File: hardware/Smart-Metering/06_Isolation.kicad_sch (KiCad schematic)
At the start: 25 parts, among them U601 ISO7741, U602 ISO7742, U603 ISO7740, U604 MCP3204, U605 TPS7A2033

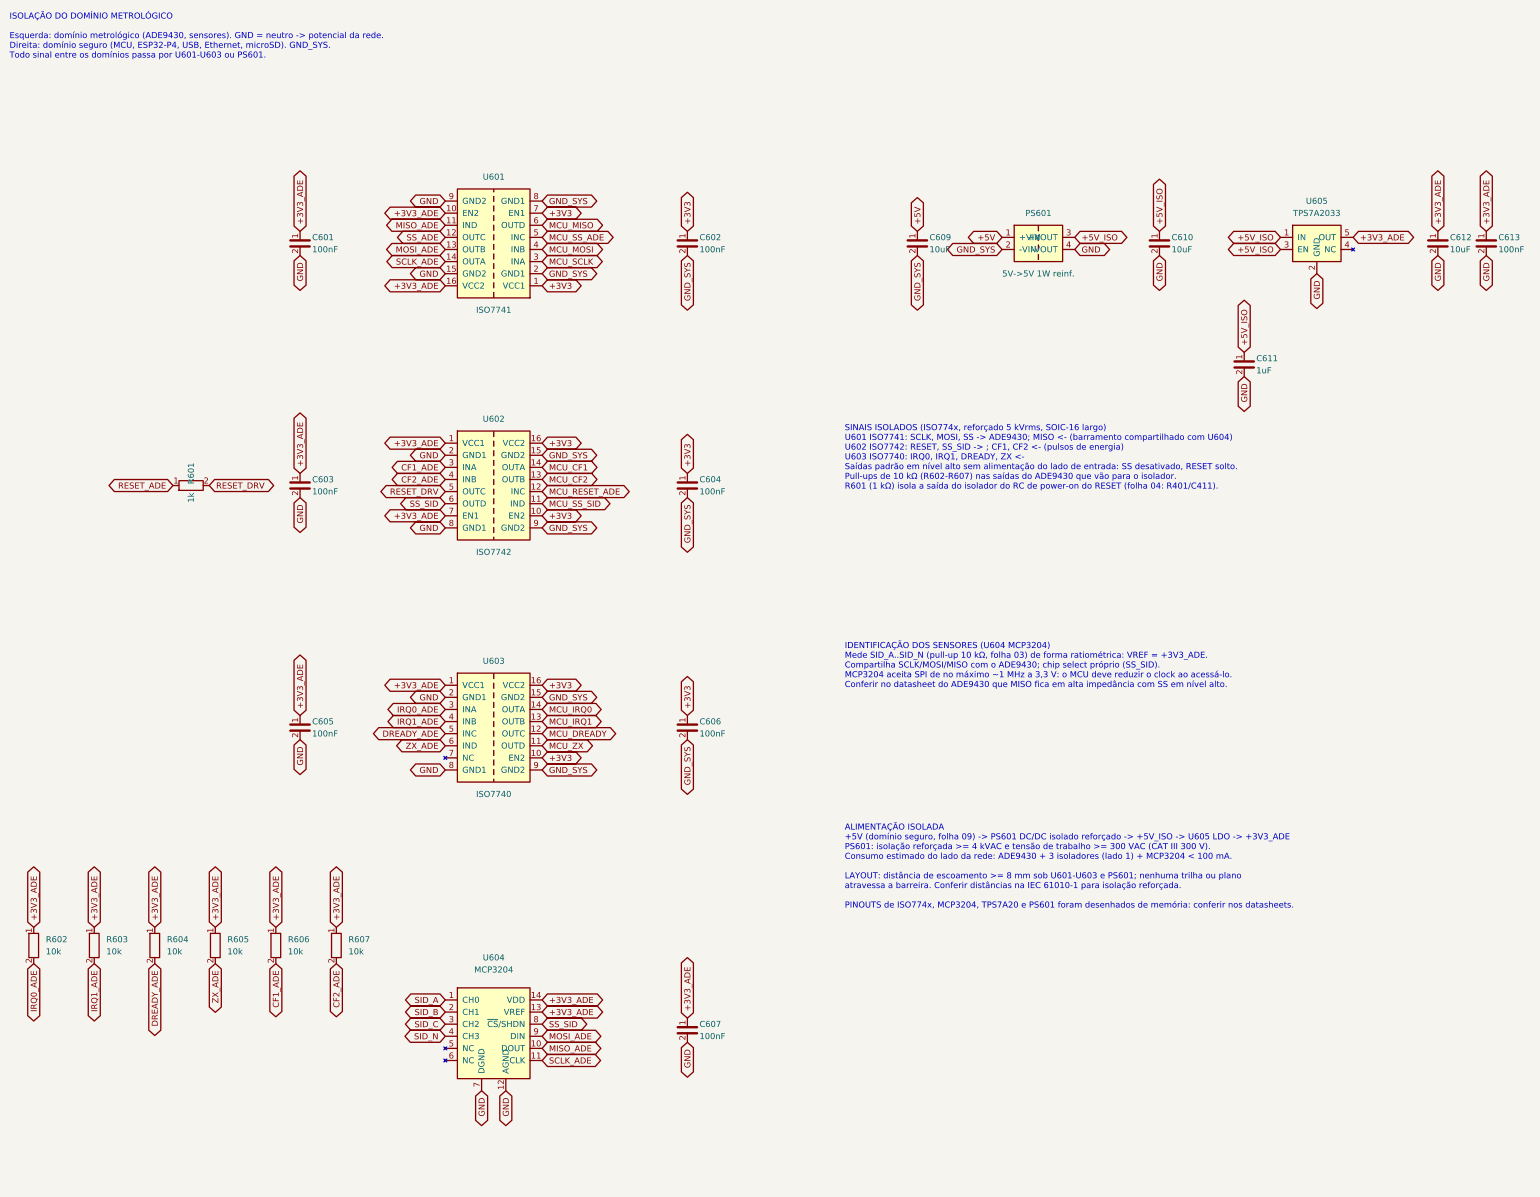
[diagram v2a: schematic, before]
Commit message: Usa símbolos oficiais do KiCad nas folhas de isolação e alimentação
Os símbolos oficiais da biblioteca KiCad 10 (gitlab.com/kicad/libraries)
substituem os desenhados de memória:

- 06_Isolation: ISO7762DW (4/2) e ISO7761DW (5/1) no lugar de três
  ISO774x; os 12 sinais cabem em dois isoladores reforçados. MCP3204 e
  TPS7A20xxxDBV oficiais (os pinouts anteriores conferiram).
- 09_Power_Supplies: BQ24074RGT oficial revelou que o pino 15 é ITERM,
  não SYSOFF; agora tem R911 (3,01 kΩ, fim de carga ≈ 90 mA). +3V3 passa
  ao TPS63001 (buck-boost 3,3 V fixo) e +5V ao TPS61089, com resistores
  de frequência, limite de corrente e compensação a confirmar no WEBENCH.

Símbolos próprios que deixaram de ser usados foram removidos da
biblioteca SmartMetering.

Co-Authored-By: Claude Opus 5.5 <noreply@anthropic.com>
Claude-Session: https://claude.ai/code/session_012B8cVkhtjf3eg98UdpNCpf
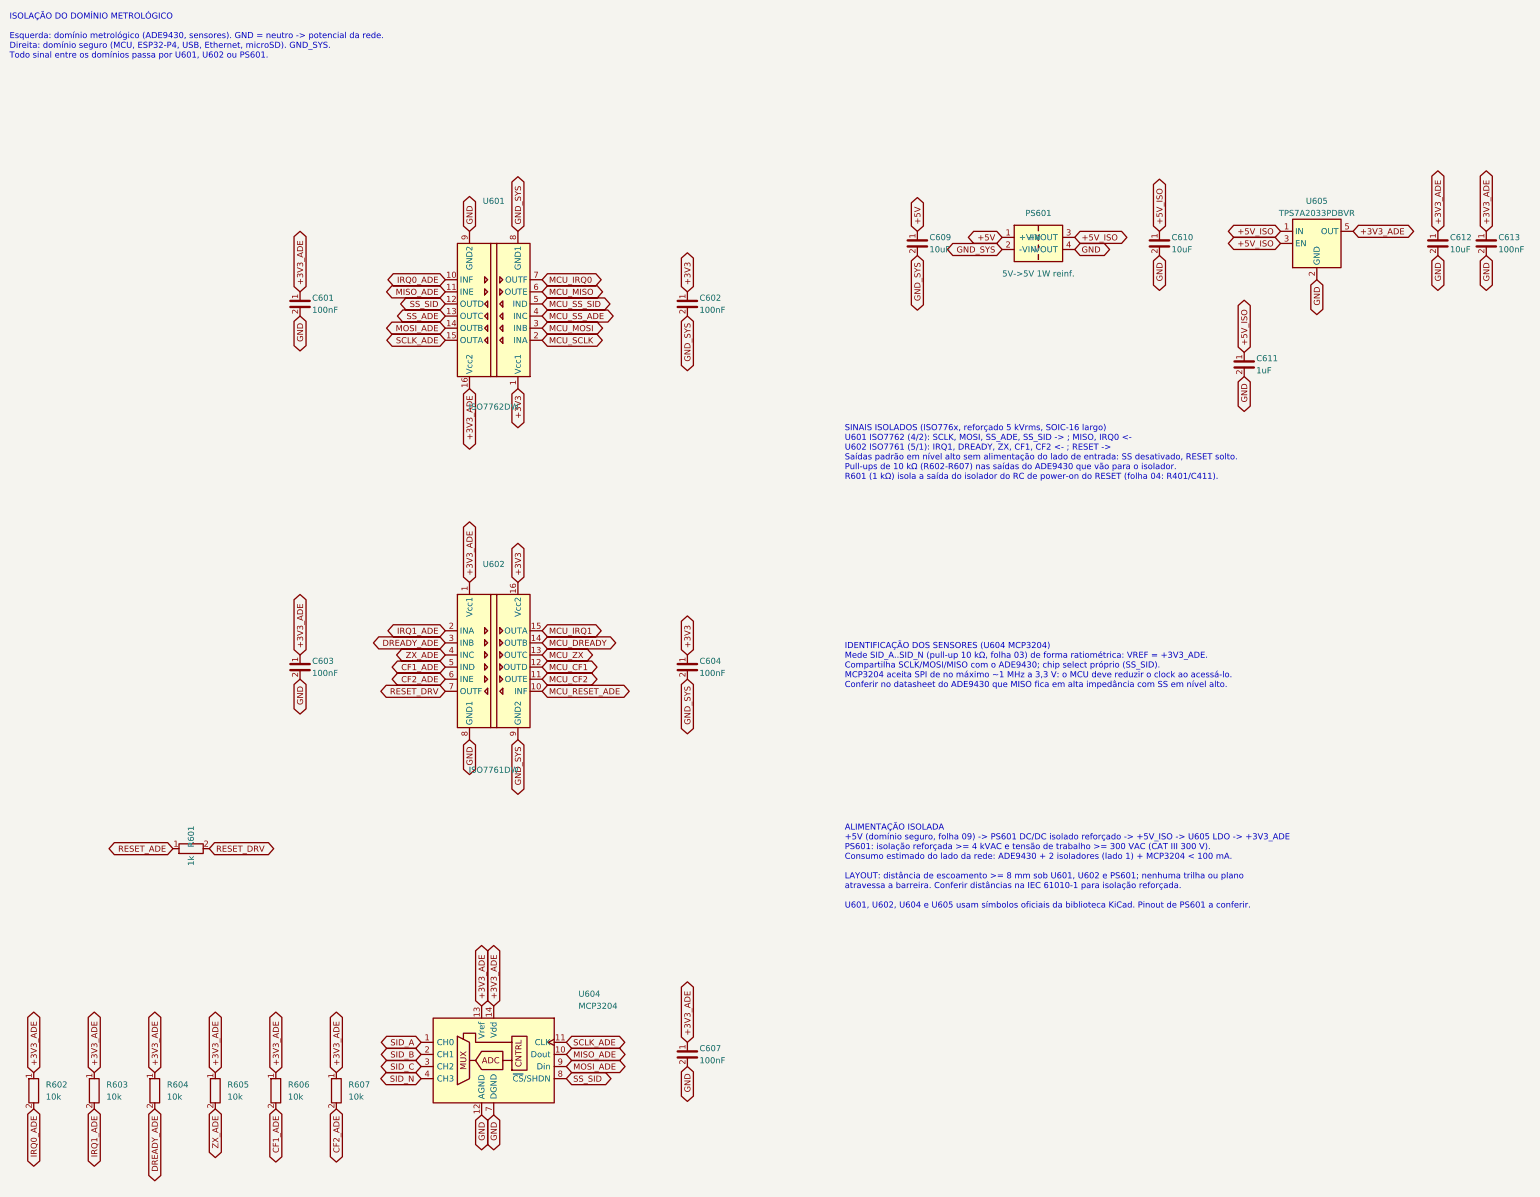
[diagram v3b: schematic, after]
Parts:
- removed C605, C606: 100nF, Capacitor_SMD:C_0603_1608Metric, symbol SmartMetering:C_Vert
- removed U601: ISO7741, Package_SO:SOIC-16W_7.5x10.3mm_P1.27mm, symbol SmartMetering:ISO7741
- removed U602: ISO7742, Package_SO:SOIC-16W_7.5x10.3mm_P1.27mm, symbol SmartMetering:ISO7742
- removed U603: ISO7740, Package_SO:SOIC-16W_7.5x10.3mm_P1.27mm, symbol SmartMetering:ISO7740
- removed U604: MCP3204, Package_SO:SOIC-14_3.9x8.7mm_P1.27mm, symbol SmartMetering:MCP3204
- removed U605: TPS7A2033, Package_TO_SOT_SMD:SOT-23-5, symbol SmartMetering:LDO_EN_SOT23-5
- added U601: ISO7762DW, Package_SO:SOIC-16W_7.5x10.3mm_P1.27mm, symbol Isolator:ISO7762DW
- added U602: ISO7761DW, Package_SO:SOIC-16W_7.5x10.3mm_P1.27mm, symbol Isolator:ISO7761DW
- added U604: MCP3204, Package_SO:SOIC-14_3.9x8.7mm_P1.27mm, symbol Analog_ADC:MCP3204
- added U605: TPS7A2033PDBVR, Package_TO_SOT_SMD:SOT-23-5, symbol Regulator_Linear:TPS7A20xxxDBV
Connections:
- net +3V3: now also U601.1 (Vcc1), U602.16 (Vcc2)
- net +3V3_ADE: now also U601.16 (Vcc2), U602.1 (Vcc1), U604.13 (Vref), U604.14 (Vdd), U605.5 (OUT)
- net +5V_ISO: now also U605.1 (IN), U605.3 (EN)
- net CF1_ADE: now also U602.5 (IND)
- net CF2_ADE: now also U602.6 (INE)
- net DREADY_ADE: now also U602.3 (INB)
- net GND: now also U601.9 (GND2), U602.8 (GND1), U604.12 (AGND), U604.7 (DGND), U605.2 (GND)
- net GND_SYS: now also U601.8 (GND1), U602.9 (GND2)
- net IRQ0_ADE: now also U601.10 (INF)
- net IRQ1_ADE: now also U602.2 (INA)
- net MCU_CF1: now also U602.12 (OUTD)
- net MCU_CF2: now also U602.11 (OUTE)
- net MCU_DREADY: now also U602.14 (OUTB)
- net MCU_IRQ0: now also U601.7 (OUTF)
- net MCU_IRQ1: now also U602.15 (OUTA)
- net MCU_MISO: now also U601.6 (OUTE)
- net MCU_MOSI: now also U601.3 (INB)
- net MCU_RESET_ADE: now also U602.10 (INF)
- net MCU_SCLK: now also U601.2 (INA)
- net MCU_SS_ADE: now also U601.4 (INC)
- net MCU_SS_SID: now also U601.5 (IND)
- net MCU_ZX: now also U602.13 (OUTC)
- net MISO_ADE: now also U601.11 (INE), U604.10 (Dout)
- net MOSI_ADE: now also U601.14 (OUTB), U604.9 (Din)
- net RESET_DRV: now also U602.7 (OUTF)
- net SCLK_ADE: now also U601.15 (OUTA), U604.11 (CLK)
- net SID_A: now also U604.1 (CH0)
- net SID_B: now also U604.2 (CH1)
- net SID_C: now also U604.3 (CH2)
- net SID_N: now also U604.4 (CH3)
- net SS_ADE: now also U601.13 (OUTC)
- net SS_SID: now also U601.12 (OUTD), U604.8 (~{CS}/SHDN)
- net ZX_ADE: now also U602.4 (INC)
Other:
- note added: "ALIMENTAÇÃO ISOLADA +5V (domínio seguro, folha 09) -> PS601 DC/DC isolado reforçado -> +5V_ISO -> U605 LDO -> +3V3_ADE PS601: isolação reforçada >= 4 kVAC e tensão de trabalho >= 300 VAC (CAT III 300 V). Consumo estimado do lado da rede: ADE9430 + 2 isoladores (lado 1) + MCP3204 < 100 mA. LAYOUT: distância de escoamento >= 8 mm sob U601, U602 e PS601; nenhuma trilha ou plano atravessa a barreira.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"
- note added: "ISOLAÇÃO DO DOMÍNIO METROLÓGICO Esquerda: domínio metrológico (ADE9430, sensores). GND = neutro -> potencial da rede. Direita: domínio seguro (MCU, ESP32-P4, USB, Ethernet, microSD). GND_SYS. Todo sinal entre os domínios passa por U601, U602 ou PS601."
- note added: "SINAIS ISOLADOS (ISO776x, reforçado 5 kVrms, SOIC-16 largo) U601 ISO7762 (4/2): SCLK, MOSI, SS_ADE, SS_SID -> ; MISO, IRQ0 <- U602 ISO7761 (5/1): IRQ1, DREADY, ZX, CF1, CF2 <- ; RESET -> Saídas padrão em nível alto sem alimentação do lado de entrada: SS desativado, RESET solto. Pull-ups de 10 kΩ (R602-R607) nas saídas do ADE9430 que vão para o isolador. R601 (1 kΩ) isola a saída do isolador do RC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"
- note removed: "ALIMENTAÇÃO ISOLADA +5V (domínio seguro, folha 09) -> PS601 DC/DC isolado reforçado -> +5V_ISO -> U605 LDO -> +3V3_ADE PS601: isolação reforçada >= 4 kVAC e tensão de trabalho >= 300 VAC (CAT III 300 V). Consumo estimado do lado da rede: ADE9430 + 3 isoladores (lado 1) + MCP3204 < 100 mA. LAYOUT: distância de escoamento >= 8 mm sob U601-U603 e PS601; nenhuma trilha ou plano atravessa a barreira. 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"
- note removed: "ISOLAÇÃO DO DOMÍNIO METROLÓGICO Esquerda: domínio metrológico (ADE9430, sensores). GND = neutro -> potencial da rede. Direita: domínio seguro (MCU, ESP32-P4, USB, Ethernet, microSD). GND_SYS. Todo sinal entre os domínios passa por U601-U603 ou PS601."
- note removed: "SINAIS ISOLADOS (ISO774x, reforçado 5 kVrms, SOIC-16 largo) U601 ISO7741: SCLK, MOSI, SS -> ADE9430; MISO <- (barramento compartilhado com U604) U602 ISO7742: RESET, SS_SID -> ; CF1, CF2 <- (pulsos de energia) U603 ISO7740: IRQ0, IRQ1, DREADY, ZX <- Saídas padrão em nível alto sem alimentação do lado de entrada: SS desativado, RESET solto. Pull-ups de 10 kΩ (R602-R607) nas saídas do ADE9430 que v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"

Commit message: Resolve as pendências da revisão do esquemático
P1  ADE9430: footprint VQFN-40 6x6 com EP de 4,15 mm, compatível com as
    variantes CP-40 de 6x6 mm (EP de 3,9 a 4,7 mm).
P2  Confirmado no datasheet: MISO solto com SS alto (pull-up de 100 kΩ)
    e NC1/NC2 em GND, como já estava.
P3  J301-J304: headers JST PH de 4 vias cabeados até conectores M8
    fêmea de painel (à prova de toque).
P4  PS601 -> U606 ADuM6000 (isoPower 5 kVrms, símbolo oficial).
P5  PS101 -> RAC20-05SK/277 (85-305 VAC, 120-430 VDC, 20 W); fusíveis
    T500mA, R101 3 W, C101 10 uF/450 V; entrada do BQ25895 a 3 A.
P7  TPS61089 -> TPS61022 (compensação interna, sem valores a ajustar).
P8  Placa EV alimentada pelos pinos 5 V do J1 (nota na folha 07).
P9  EEPROM de calibração 24LC64 no I2C1.
P10 Labels globais de uma só folha convertidos em locais.

Verificação: 223 componentes, nenhum pino solto, nenhuma net sem fonte,
nenhum conflito de saída, isolação íntegra, todos os footprints
existentes na biblioteca oficial do KiCad.

Co-Authored-By: Claude Opus 5.5 <noreply@anthropic.com>
Claude-Session: https://claude.ai/code/session_012B8cVkhtjf3eg98UdpNCpf
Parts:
- removed PS601: 5V->5V 1W reinf., symbol SmartMetering:DCDC_Isolated
- added C614, C615, C616: 100nF, Capacitor_SMD:C_0603_1608Metric, symbol SmartMetering:C_Vert
- added U606: ADuM6000, Package_SO:SOIC-16W_7.5x10.3mm_P1.27mm, symbol Converter_DCDC_Isolated:ADuM6000
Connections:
- net +5V: now also C614.1, C615.1, U606.1 (VDD1), U606.6 (RC_SEL), U606.7 (VDD1)
- net +5V_ISO: now also C616.1, U606.10 (V_ISO), U606.13 (V_SEL), U606.16 (V_ISO)
- net GND: now also C616.2, U606.15 (GND_ISO), U606.9 (GND_ISO)
- net GND_SYS: now also C614.2, C615.2, U606.2 (GND1), U606.4 (RC_IN), U606.8 (GND1)
- no-connect marks 0 -> 1
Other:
- note added: "ALIMENTAÇÃO ISOLADA +5V (domínio seguro, folha 09) -> U606 ADuM6000 (isoPower) -> +5V_ISO -> U605 LDO -> +3V3_ADE U606: 5 kVrms; RC_SEL em VDD1 e RC_IN em GND1 (regulação interna), V_SEL em V_ISO (5 V). Confirmar no datasheet a certificação reforçada e a tensão de trabalho para CAT III 300 V. isoPower comuta em alta frequência: seguir as regras de layout/EMI do datasheet (capacitância de costura)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"
- note added: "ISOLAÇÃO DO DOMÍNIO METROLÓGICO Esquerda: domínio metrológico (ADE9430, sensores). GND = neutro -> potencial da rede. Direita: domínio seguro (MCU, ESP32-P4, USB, Ethernet, microSD). GND_SYS. Todo sinal entre os domínios passa por U601, U602 ou U606."
- note removed: "ALIMENTAÇÃO ISOLADA +5V (domínio seguro, folha 09) -> PS601 DC/DC isolado reforçado -> +5V_ISO -> U605 LDO -> +3V3_ADE PS601: isolação reforçada >= 4 kVAC e tensão de trabalho >= 300 VAC (CAT III 300 V). Consumo estimado do lado da rede: ADE9430 + 2 isoladores (lado 1) + MCP3204 < 100 mA. LAYOUT: distância de escoamento >= 8 mm sob U601, U602 e PS601; nenhuma trilha ou plano atravessa a barreira.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"
- note removed: "ISOLAÇÃO DO DOMÍNIO METROLÓGICO Esquerda: domínio metrológico (ADE9430, sensores). GND = neutro -> potencial da rede. Direita: domínio seguro (MCU, ESP32-P4, USB, Ethernet, microSD). GND_SYS. Todo sinal entre os domínios passa por U601, U602 ou PS601."
